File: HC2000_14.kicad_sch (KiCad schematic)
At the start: 55 parts, among them J1 VIDEO, J10 SDS-60J, J2 JOYSTICK, J3 MAB5SH, J4 ., J5 RS232 + RETEA, J6 ., J7 FDD-CON, J8 FDD-CON, J9 .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

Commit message: Fix errors (IC & unnoticed cut for 1 EPROM)
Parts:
- UA1: value 74244N -> 74LS244
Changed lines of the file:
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@@
       (effects (font (size 1.778 1.5113)) (justify left bottom))
     )
-    (property "Value" "74244N" (at 55.88 48.26 0)
+    (property "Value" "74LS244" (at 55.88 48.26 0)
       (effects (font (size 1.778 1.5113)) (justify left bottom))
     )
@@
       (effects (font (size 1.778 1.5113)) (justify left bottom))
     )
-    (property "Value" "74244N" (at 55.88 73.66 0)
-      (effects (font (size 1.778 1.5113)) (justify left bottom))
-    )
+    (property "Value" "74LS244" (at 55.88 73.66 0)
+      (effects (font (size 1.778 1.5113)) (justify left bottom))
+    )

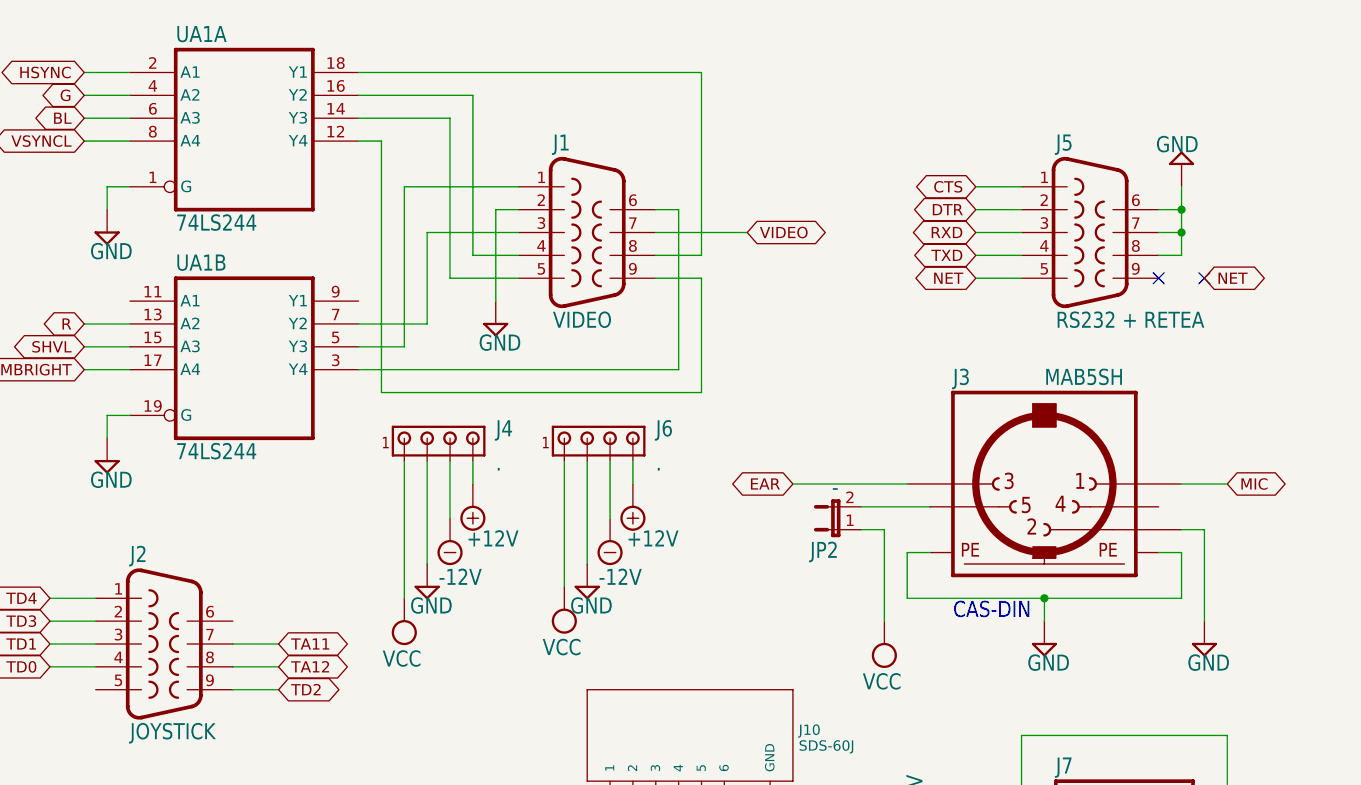
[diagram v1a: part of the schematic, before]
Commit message: A few minor changes
R62 has value 470 instead of 910 and C6 is missing.
Connected a few conector's shield pins to GND.
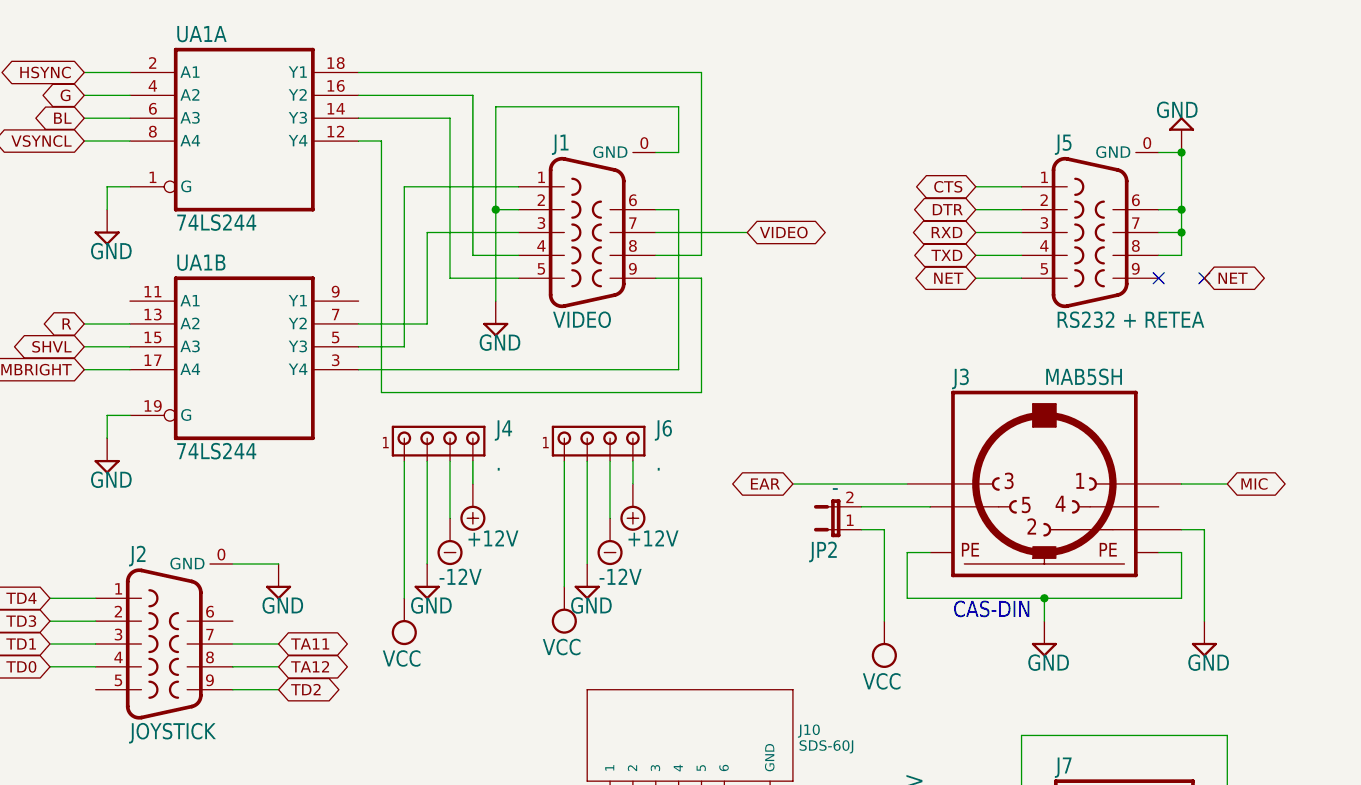
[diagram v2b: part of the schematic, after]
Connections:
- net GND: now also J1.0 (GND), J2.0 (GND), J5.0 (GND)

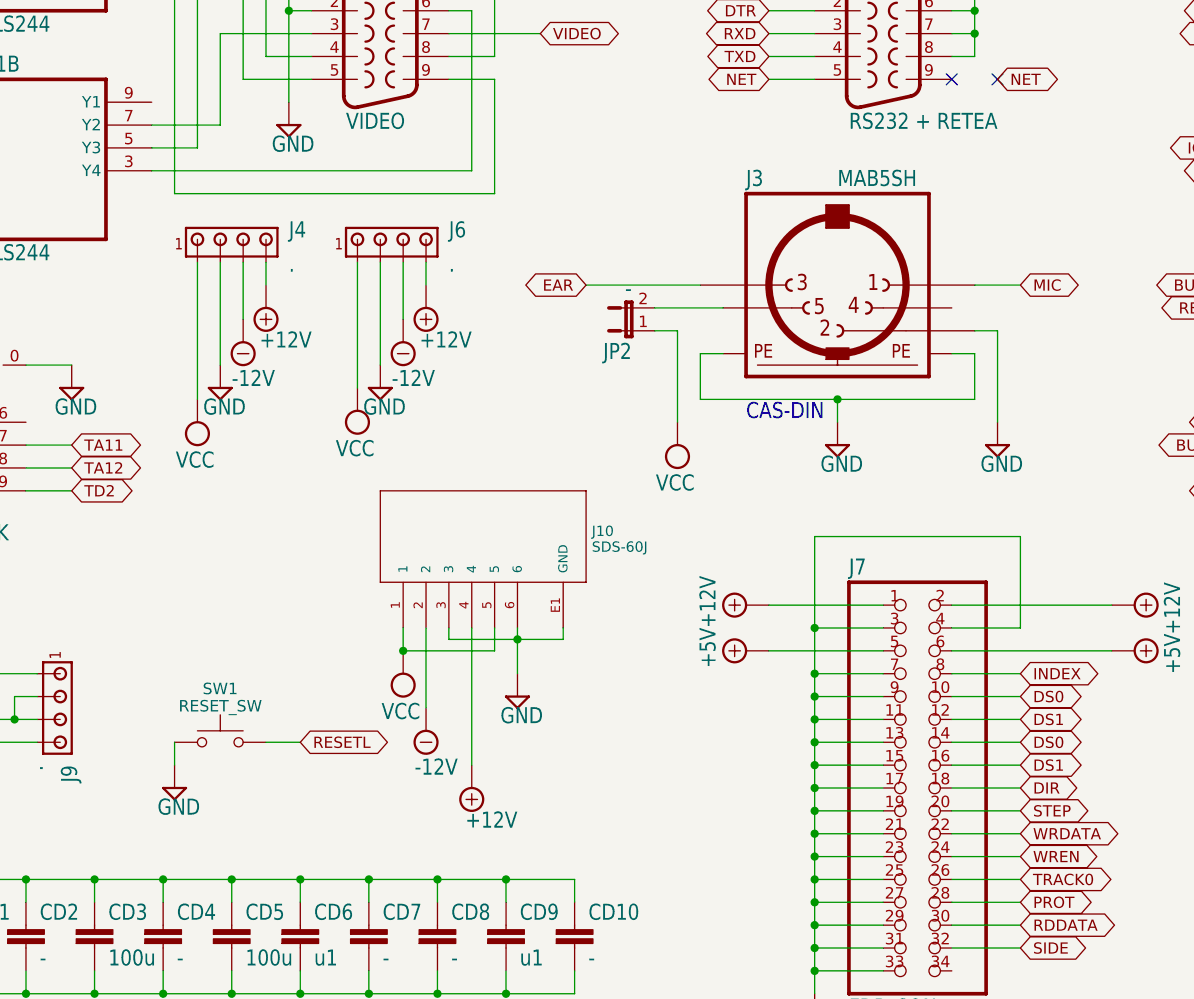
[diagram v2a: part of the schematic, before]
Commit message: Updated power, audio and keyboard connectors
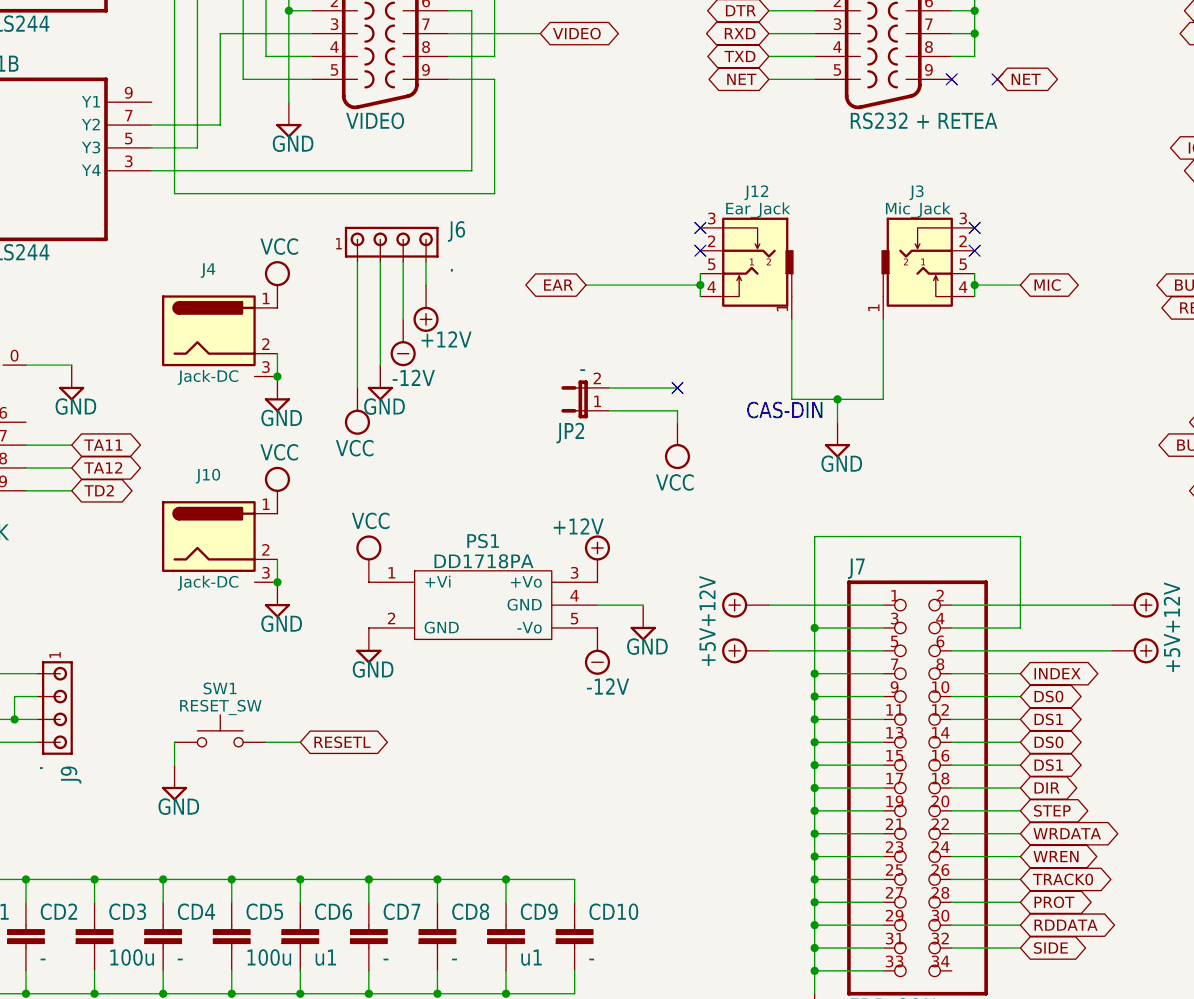
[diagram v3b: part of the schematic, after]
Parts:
- removed J10: SDS-60J, HC2000:SDS-60J-CUI_SDS-60J, symbol HC2000:SDS-60J
- removed J3: MAB5SH, HC2000:MAB5SH, symbol HC2000:MAB5SH
- removed J4: ., HC2000:HC-POWER, symbol HC2000:HC-POWER
- added J10, J4: Jack-DC, HC2000:BarrelJack_Wuerth_6941xx301002, symbol HC2000:Jack-DC
- added J12: Ear_Jack, HC2000:Tayda_3.5mm_stereo_TRS_jack_A-853, symbol HC2000:Audio-Jack-3_2Switches
- added J3: Mic_Jack, HC2000:Tayda_3.5mm_stereo_TRS_jack_A-853, symbol HC2000:Audio-Jack-3_2Switches
- added PS1: DD1718PA, HC2000:DD1718PA, symbol HC2000:DD1718PA
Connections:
- net +12V: now also PS1.3 (+Vo)
- net -12V: now also PS1.5 (-Vo)
- net EAR: now also J12.4, J12.5
- net GND: now also J10.2, J10.3, J12.1, J3.1, J4.2, J4.3, PS1.2 (GND), PS1.4 (GND)
- net MIC: now also J3.4, J3.5
- net VCC: now also J10.1, J4.1, PS1.1 (+Vi)
- no-connect marks 2 -> 7
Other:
- moved on the sheet: JP2
